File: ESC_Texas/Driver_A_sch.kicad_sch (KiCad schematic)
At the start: 25 parts, among them IC1 UCC21331CQDRQ1, Q1 IPD100N06S4, Q2 IPD100N06S4

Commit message: Initial design
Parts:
- C_IN1, C_IN2, C_IN3: value C -> 33pF
- C_VDD_B1: value C -> 10uF
- RR_ON_B1, R_ON_A1: value R -> 4.7
- R_BOOT_A1: value R -> 6.8
- R_DT1: value R -> 20k
- R_GS_A1, R_GS_B1: value R -> 10k
- R_INA1, R_INB1: value R -> 47
- R_OFF_A1: value R -> 0
- R_OFF_B1: value R -> R=0
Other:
- note added: "R_BOOT: 1-20R. Page 25 R_BOOT = 6.8 Ohm"
- note added: "R_GS: 5.1k - 20k R_GS = 10K"
- note added: "R_ON High: 5R. Page 8 R_ON = 4.7"
- note removed: "R_BOOT: 1-20R. Page 25"
- note removed: "R_GS: 5.1k - 20k"
- note removed: "R_ON High: 5R. Page 8"
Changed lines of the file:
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@@
 		)
 	)
-	(text "R_BOOT: 1-20R. Page 25"
+	(text "R_BOOT: 1-20R. Page 25\nR_BOOT = 6.8 Ohm"
 		(exclude_from_sim no)
 		(at 168.148 46.736 0)
@@
 		)
 	)
-	(text "R_GS: 5.1k - 20k "
+	(text "R_GS: 5.1k - 20k \nR_GS = 10K"
 		(exclude_from_sim no)
 		(at 199.644 37.338 0)
@@
 		)
 	)
-	(text "R_ON High: 5R. Page 8"
+	(text "R_ON High: 5R. Page 8\nR_ON = 4.7"
 		(exclude_from_sim no)
 		(at 200.914 44.196 0)
@@
 			)
 		)
-		(property "Value" "C"
+		(property "Value" "33pF"
 			(at 88.138 88.9 0)
 			(effects
@@
 			)
 		)
-		(property "Value" "R"
+		(property "Value" "6.8"
 			(at 166.624 68.834 90)
 			(effects
@@
 			)
 		)
-		(property "Value" "R"
+		(property "Value" "4.7"
 			(at 196.85 115.824 90)
 			(effects
@@
 			)
 		)
-		(property "Value" "R"
+		(property "Value" "47"
 			(at 66.04 68.326 90)
 			(effects
@@
 			)
 		)
-		(property "Value" "C"
+		(property "Value" "33pF"
 			(at 243.84 77.4699 0)
 			(effects
@@
 			)
 		)
-		(property "Value" "R"
+		(property "Value" "0"
 			(at 196.85 66.04 90)
 			(effects
@@
 			)
 		)
-		(property "Value" "R"
+		(property "Value" "10k"
 			(at 208.28 87.6299 0)
 			(effects
@@
 			)
 		)
-		(property "Value" "R"
+		(property "Value" "47"
 			(at 66.04 76.708 90)
 			(effects
@@
 			)
 		)
-		(property "Value" "R"
+		(property "Value" "10k"
 			(at 208.28 116.8399 0)
 			(effects
@@
 			)
 		)
-		(property "Value" "R"
+		(property "Value" "4.7"
 			(at 198.12 78.994 90)
 			(effects
@@
 			)
 		)
-		(property "Value" "R"
+		(property "Value" "R=0"
 			(at 196.85 100.33 90)
 			(effects
@@
 			)
 		)
-		(property "Value" "C"
+		(property "Value" "33pF"
 			(at 99.314 86.106 0)
 			(effects
@@
 			)
 		)
-		(property "Value" "R"
+		(property "Value" "20k"
 			(at 137.414 105.41 0)
 			(effects
@@
 			)
 		)
-		(property "Value" "C"
+		(property "Value" "10uF"
 			(at 181.61 104.1399 0)
 			(effects

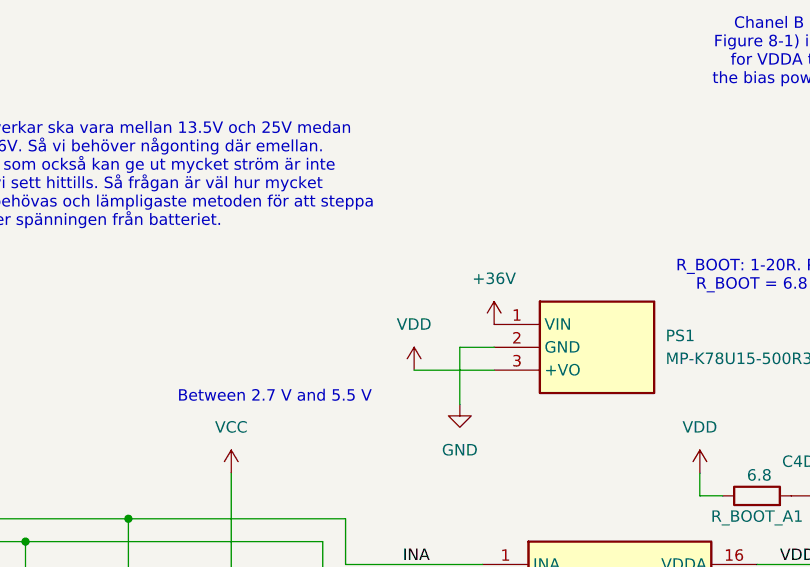
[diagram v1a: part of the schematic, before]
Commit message: Added text: VDD=15V
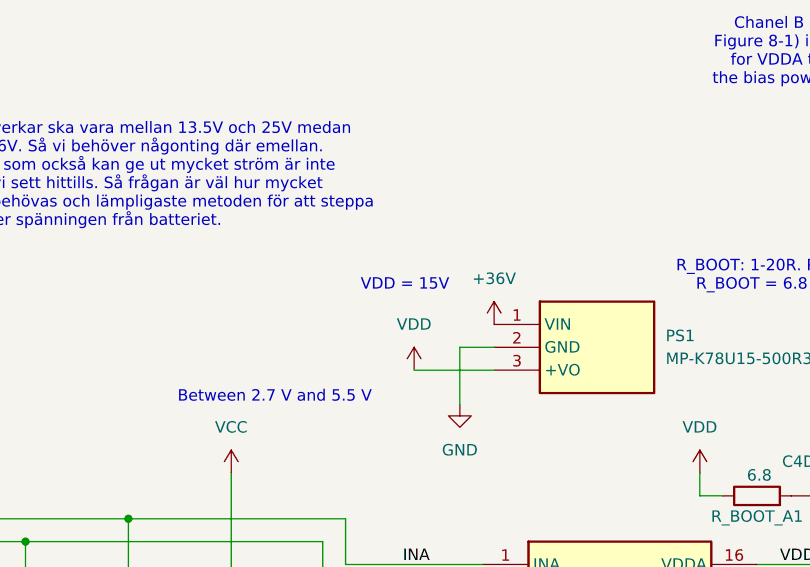
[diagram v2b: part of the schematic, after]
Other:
- note added: "VDD = 15V"
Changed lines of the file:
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@@
+		)
+	)
+	(text "VDD = 15V"
+		(exclude_from_sim no)
+		(at 127.254 47.752 0)
+		(effects
+			(font
+				(size 1.27 1.27)
+			)
 		)
 	)

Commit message: Saved project after footprints/symbols addition
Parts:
- IC1: footprint UCC21331CDR:SOIC127P600X175-16N -> LIB_UCC21331CQDRQ1:SOIC127P600X175-16N
- PS1: footprint MPK78U15500R3L -> MP-K78U15-500R3L:MPK78U15500R3L
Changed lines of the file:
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@@
 			)
 		)
-		(property "Footprint" "MPK78U15500R3L"
+		(property "Footprint" "MP-K78U15-500R3L:MPK78U15500R3L"
 			(at 156.21 146.99 0)
 			(effects
@@
 			)
 		)
-		(property "Footprint" "UCC21331CDR:SOIC127P600X175-16N"
+		(property "Footprint" "LIB_UCC21331CQDRQ1:SOIC127P600X175-16N"
 			(at 162.56 173.66 0)
 			(effects

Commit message: Save
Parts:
- renumbered D4 to D3, PS1 to PS2, Q1 to Q3

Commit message: Before adding footprint
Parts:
- renumbered C_BOOT_A1 to C_BOOT_A3, C_DT1 to C_DT3, C_EN1 to C_EN3, C_IN1 to C_IN7, C_IN2 to C_IN8, C_IN3 to C_IN9, C_VCC1 to C_VCC5, C_VDD_B1 to C_VDD_B3, D2 to D7, D3 to D8, D5 to D9, IC1 to IC3, PS2 to PS3, Q3 to Q5, Q2 to Q6, RR_ON_B1 to RR_ON_B3, R_BOOT_A1 to R_BOOT_A3, R_DT1 to R_DT3, R_GS_A1 to R_GS_A3, R_GS_B1 to R_GS_B3, R_INA1 to R_INA3, R_INB1 to R_INB3, R_OFF_A1 to R_OFF_A3, R_OFF_B1 to R_OFF_B3, R_ON_A1 to R_ON_A3
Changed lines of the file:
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@@
 		(dnp no)
 		(fields_autoplaced yes)
-		(property "Reference" "D3"
+		(property "Reference" "D8"
 			(at 207.01 63.5 0)
 			(effects
@@
 					(unit 1)
 				)
+				(path "/485715ad-2455-40db-a806-c2c62ef6f5e1/7586262d-272d-4a40-b2fe-a7f505e9f1d4"
+					(reference "D8")
+					(unit 1)
+				)
 				(path "/485715ad-2455-40db-a806-c2c62ef6f5e1/80faa729-a5f2-4405-b737-e1a1931e176c"
 					(reference "D3")
@@
 		(dnp no)
 		(fields_autoplaced yes)
-		(property "Reference" "#PWR013"
+		(property "Reference" "#PWR050"
 			(at 160.02 72.39 0)
 			(effects
@@
 		(dnp no)
 		(fields_autoplaced yes)
-		(property "Reference" "#PWR011"
+		(property "Reference" "#PWR043"
 			(at 102.87 113.03 0)
 			(effects
@@
 		(on_board yes)
 		(dnp no)
-		(property "Reference" "C_IN1"
+		(property "Reference" "C_IN7"
 			(at 88.138 85.09 0)
 			(effects
@@
 		(dnp no)
 		(fields_autoplaced yes)
-		(property "Reference" "#PWR03"
+		(property "Reference" "#PWR049"
 			(at 137.16 55.88 0)
 			(effects
@@
 		(on_board yes)
 		(dnp no)
-		(property "Reference" "R_BOOT_A1"
+		(property "Reference" "R_BOOT_A3"
 			(at 166.37 73.406 90)
 			(effects
@@
 		(dnp no)
 		(fields_autoplaced yes)
-		(property "Reference" "#PWR016"
+		(property "Reference" "#PWR053"
 			(at 219.71 68.58 0)
 			(effects
@@
 		(dnp no)
 		(fields_autoplaced yes)
-		(property "Reference" "#PWR04"
+		(property "Reference" "#PWR046"
 			(at 128.27 60.96 0)
 			(effects
@@
 		(dnp no)
 		(fields_autoplaced yes)
-		(property "Reference" "D2"
+		(property "Reference" "D7"
 			(at 174.3075 64.77 0)
 			(effects
@@
 		(dnp no)
 		(fields_autoplaced yes)
-		(property "Reference" "#PWR010"
+		(property "Reference" "#PWR044"
 			(at 107.95 72.39 0)
 			(effects
@@
 		(on_board yes)
 		(dnp no)
-		(property "Reference" "RR_ON_B1"
+		(property "Reference" "RR_ON_B3"
 			(at 196.85 113.284 90)
 			(effects
@@
 		(dnp no)
 		(fields_autoplaced yes)
-		(property "Reference" "PS2"
+		(property "Reference" "PS3"
 			(at 156.21 53.3399 0)
 			(effects
@@
 					(unit 1)
 				)
+				(path "/485715ad-2455-40db-a806-c2c62ef6f5e1/7586262d-272d-4a40-b2fe-a7f505e9f1d4"
+					(reference "PS3")
+					(unit 1)
+				)
 				(path "/485715ad-2455-40db-a806-c2c62ef6f5e1/80faa729-a5f2-4405-b737-e1a1931e176c"
 					(reference "PS2")
@@
 		(on_board yes)
 		(dnp no)
-		(property "Reference" "R_INA1"
+		(property "Reference" "R_INA3"
 			(at 66.04 65.786 90)
 			(effects
@@
 		(dnp no)
 		(fields_autoplaced yes)
-		(property "Reference" "C_IN3"
+		(property "Reference" "C_IN9"
 			(at 243.84 74.9299 0)
 			(effects
@@
 		(on_board yes)
 		(dnp no)
-		(property "Reference" "R_OFF_A1"
+		(property "Reference" "R_OFF_A3"
 			(at 196.85 63.5 90)
 			(effects
@@
 		(on_board yes)
 		(dnp no)
-		(property "Reference" "#PWR015"
+		(property "Reference" "#PWR052"
 			(at 177.8 96.52 0)
 			(effects
@@
 		(on_board yes)
 		(dnp no)
-		(property "Reference" "C_VCC1"
+		(property "Reference" "C_VCC5"
 			(at 110.744 86.36 0)
 			(effects
@@
 		(dnp no)
 		(fields_autoplaced yes)
-		(property "Reference" "R_GS_A1"
+		(property "Reference" "R_GS_A3"
 			(at 208.28 85.0899 0)
 			(effects
@@
 		(dnp no)
 		(fields_autoplaced yes)
-		(property "Reference" "Q3"
+		(property "Reference" "Q5"
 			(at 222.25 80.0099 0)
 			(effects
@@
 					(unit 1)
 				)
+				(path "/485715ad-2455-40db-a806-c2c62ef6f5e1/7586262d-272d-4a40-b2fe-a7f505e9f1d4"
+					(reference "Q5")
+					(unit 1)
+				)
 				(path "/485715ad-2455-40db-a806-c2c62ef6f5e1/80faa729-a5f2-4405-b737-e1a1931e176c"
 					(reference "Q3")
@@
 		(on_board yes)
 		(dnp no)
-		(property "Reference" "R_INB1"
+		(property "Reference" "R_INB3"
 			(at 66.04 74.168 90)
 			(effects
@@
 		(on_board yes)
 		(dnp no)
-		(property "Reference" "IC1"
+		(property "Reference" "IC3"
 			(at 150.622 104.14 0)
 			(effects
@@
 		(dnp no)
 		(fields_autoplaced yes)
-		(property "Reference" "#PWR05"
+		(property "Reference" "#PWR047"
 			(at 133.35 67.31 0)
 			(effects
@@
 		(on_board yes)
 		(dnp no)
-		(property "Reference" "C_DT1"
+		(property "Reference" "C_DT3"
 			(at 118.618 104.14 0)
 			(effects
@@
 		(on_board yes)
 		(dnp no)
-		(property "Reference" "C_BOOT_A1"
+		(property "Reference" "C_BOOT_A3"
 			(at 191.77 86.3599 0)
 			(effects
@@
 		(dnp no)
 		(fields_autoplaced yes)
-		(property "Reference" "D5"
+		(property "Reference" "D9"
 			(at 207.01 97.79 0)
 			(effects
@@
 		(on_board yes)
 		(dnp no)
-		(property "Reference" "C_EN1"
+		(property "Reference" "C_EN3"
 			(at 105.664 101.6 0)
 			(effects
@@
 		(on_board yes)
 		(dnp no)
-		(property "Reference" "R_GS_B1"
+		(property "Reference" "R_GS_B3"
 			(at 208.28 114.2999 0)
 			(effects
@@
 		(on_board yes)
 		(dnp no)
-		(property "Reference" "R_ON_A1"
+		(property "Reference" "R_ON_A3"
 			(at 198.12 76.708 90)
 			(effects
@@
 		(dnp no)
 		(fields_autoplaced yes)
-		(property "Reference" "#PWR014"
+		(property "Reference" "#PWR051"
 			(at 171.45 127 0)
 			(effects
@@
 		(dnp no)
 		(fields_autoplaced yes)
-		(property "Reference" "R_OFF_B1"
+		(property "Reference" "R_OFF_B3"
 			(at 196.85 97.79 90)
 			(effects
@@
 		(dnp no)
 		(fields_autoplaced yes)
-		(property "Reference" "Q2"
+		(property "Reference" "Q6"
 			(at 222.25 109.2199 0)
 			(effects
@@
 		(on_board yes)
 		(dnp no)
-		(property "Reference" "C_IN2"
+		(property "Reference" "C_IN8"
 			(at 99.314 82.296 0)
 			(effects
@@
 		(dnp no)
 		(fields_autoplaced yes)
-		(property "Reference" "#PWR012"
+		(property "Reference" "#PWR048"
 			(at 133.35 116.84 0)
 			(effects
@@
 		(on_board yes)
 		(dnp no)
-		(property "Reference" "R_DT1"
+		(property "Reference" "R_DT3"
 			(at 137.414 107.95 0)
 			(effects
@@
 		(dnp no)
 		(fields_autoplaced yes)
-		(property "Reference" "#PWR02"
+		(property "Reference" "#PWR045"
 			(at 125.73 116.84 0)
 			(effects
@@
 		(dnp no)
 		(fields_autoplaced yes)
-		(property "Reference" "#PWR09"
+		(property "Reference" "#PWR042"
 			(at 102.87 99.06 0)
 			(effects
@@
 		(dnp no)
 		(fields_autoplaced yes)
-		(property "Reference" "#PWR01"
+		(property "Reference" "#PWR054"
 			(at 240.03 86.36 0)
 			(effects
@@
 		(on_board yes)
 		(dnp no)
-		(property "Reference" "C_VDD_B1"
+		(property "Reference" "C_VDD_B3"
 			(at 181.61 101.5999 0)
 			(effects

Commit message: Cleaned schamatic again
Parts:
- renumbered C_BOOT_A3 to C_BOOT_A1, C_DT3 to C_DT1, C_EN3 to C_EN1, C_IN7 to C_IN1, C_IN8 to C_IN2, C_IN9 to C_IN3, C_VCC5 to C_VCC1, C_VDD_B3 to C_VDD_B1, D7 to D2, D9 to D5, IC3 to IC1, Q6 to Q2, RR_ON_B3 to RR_ON_B1, R_BOOT_A3 to R_BOOT_A1, R_DT3 to R_DT1, R_GS_A3 to R_GS_A1, R_GS_B3 to R_GS_B1, R_INA3 to R_INA1, R_INB3 to R_INB1, R_OFF_A3 to R_OFF_A1, R_OFF_B3 to R_OFF_B1, R_ON_A3 to R_ON_A1
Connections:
- net VDD renamed +15V
